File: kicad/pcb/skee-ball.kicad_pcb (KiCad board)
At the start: 2 copper layers, 106.8 x 104 mm, 61 parts, among them J13 HEADER, J18 DC_DRIVER, J19 JOYSTICK, J2 EXTERNAL_BUTTON, J20 SERVO, J21 US0, J22 US1, J26 US2, J27 US3, J3 Conn_02x06_Counter_Clockwise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

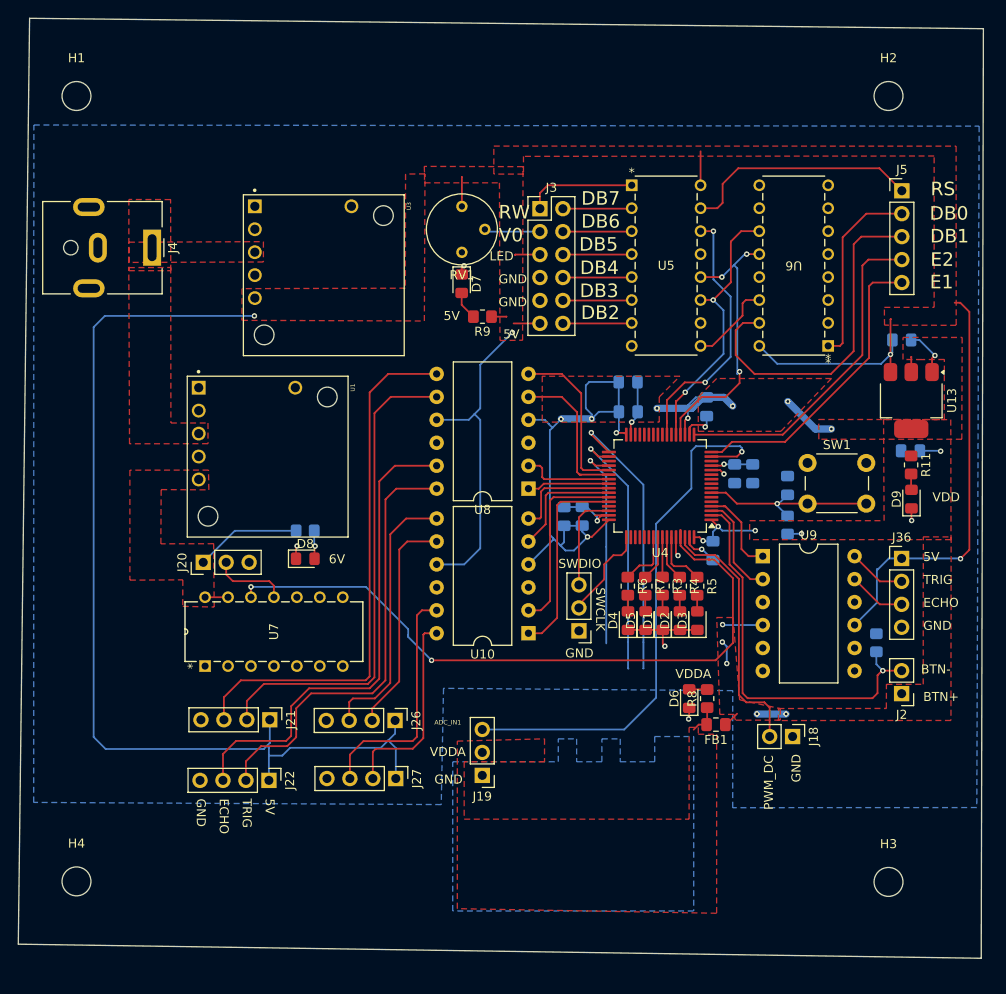
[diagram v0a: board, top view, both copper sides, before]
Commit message: only one drc error left
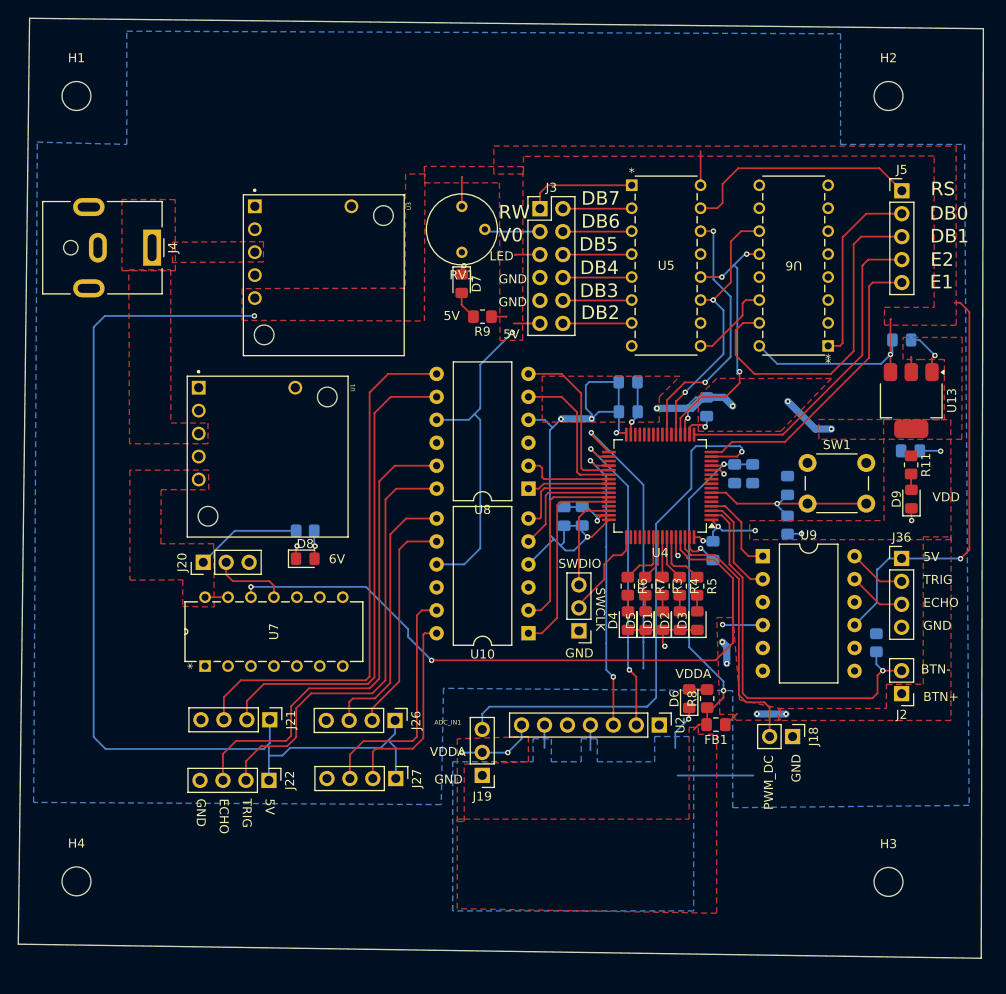
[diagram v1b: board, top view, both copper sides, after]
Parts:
- added U2: MAX98357A, Connector_PinHeader_2.54mm:PinHeader_1x07_P2.54mm_Vertical, F.Cu at (135.1, 99.1)
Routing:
- net VDDA: track 8.21 -> 48.2 mm, vias 1 -> 4
- net GND: track 44.2 -> 62.1 mm
- net SPI2-MOSI(I2S_SD): track 23.3 -> 32.7 mm, vias 1 -> 2
- net SPI2-SCK(I2S_CK): track 28.4 -> 34.8 mm, vias 1 -> 2
- net PWM_SERVO_3.3: track 76.4 -> 75.1 mm
- net ADC_IN1: track 59.5 -> 60.5 mm

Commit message: fix pcb dimensions
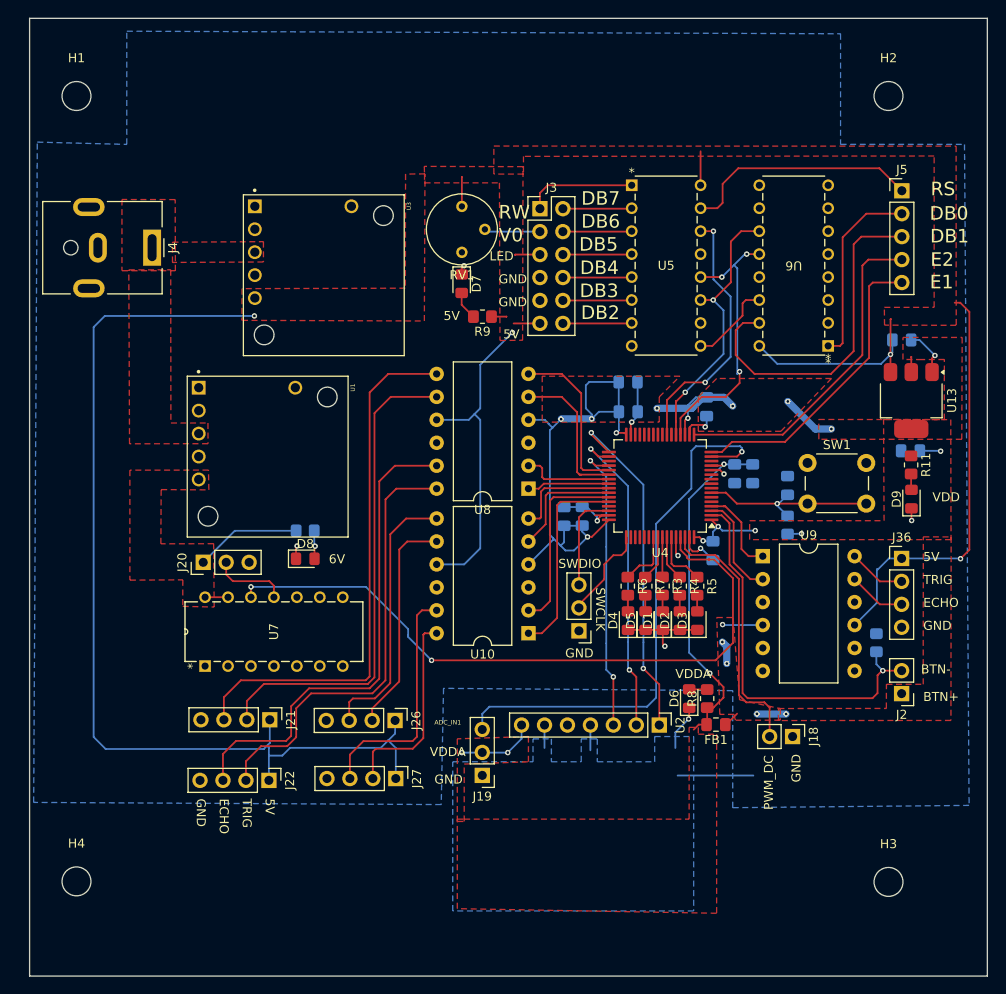
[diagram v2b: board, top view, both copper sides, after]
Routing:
- net SPI2-NSS(I2S_WS): track 31.4 -> 38.4 mm, vias 1 -> 2
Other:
- board size 106.8 x 104 mm -> 106 x 106 mm

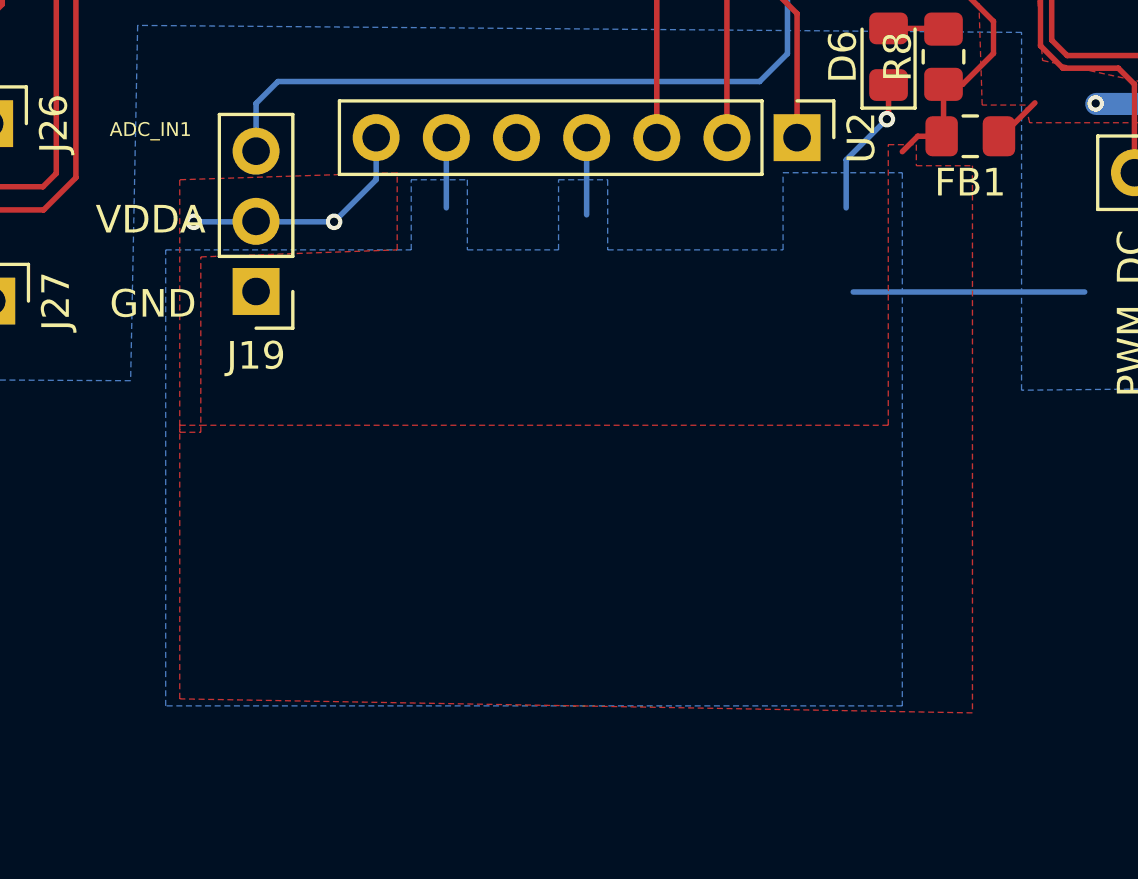
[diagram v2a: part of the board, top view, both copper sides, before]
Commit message: reorganize schematic and fix max98357a pins
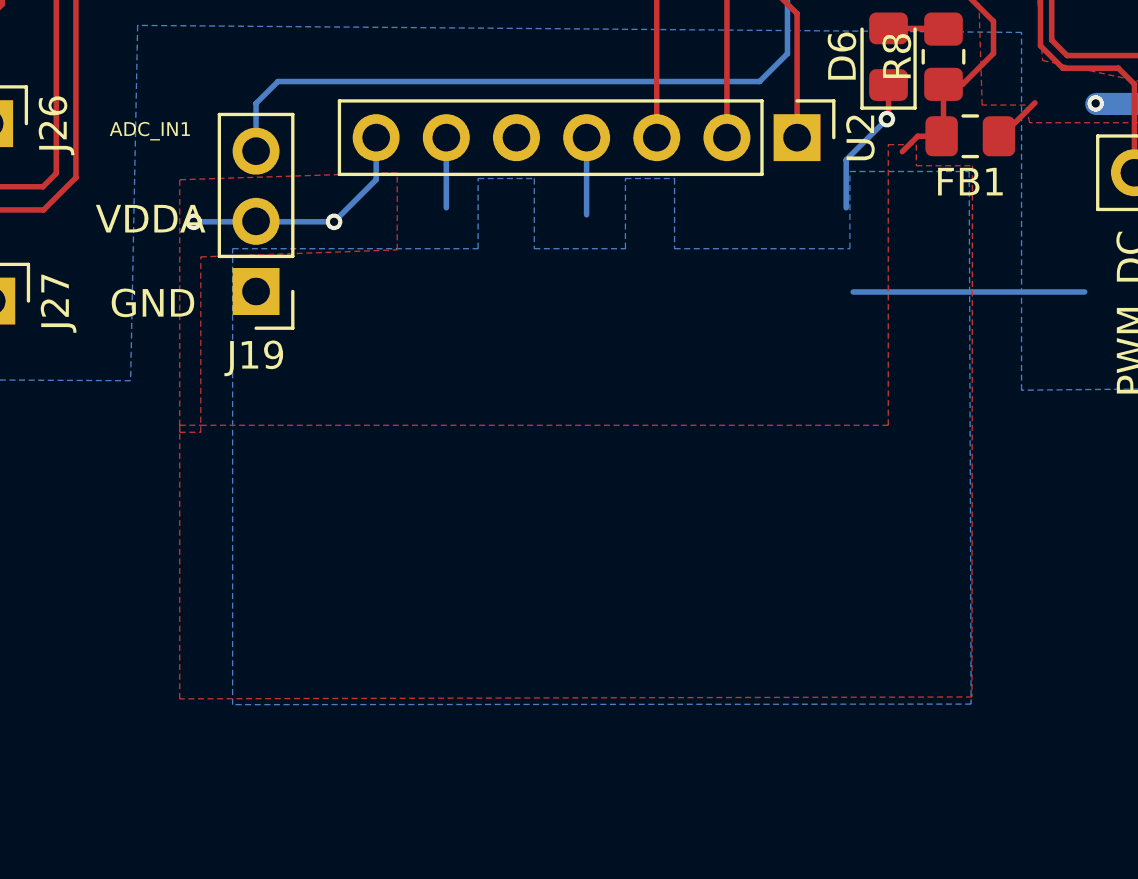
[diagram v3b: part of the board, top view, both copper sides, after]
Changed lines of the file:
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@@
 			(remove_unused_layers no)
 			(net 3 "GND")
-			(pinfunction "GAIN")
+			(pinfunction "GAIN_SLOT")
 			(pintype "passive")
 		)
@@
 		(min_thickness 0.25)
 		(filled_areas_thickness no)
-		(fill yes
+		(fill
 			(thermal_gap 0.5)
 			(thermal_bridge_width 0.5)
@@
 		(polygon
 			(pts
-				(xy 138.43 99.314) (xy 139.446 99.314) (xy 139.446 100.076) (xy 141.478 100.076) (xy 141.478 119.888)
+				(xy 138.43 99.314) (xy 139.446 99.314) (xy 139.446 100.076) (xy 141.478 100.076) (xy 141.46 119.31)
 				(xy 112.776 119.38) (xy 112.776 109.474) (xy 113.538 109.474) (xy 138.43 109.474)
 			)
@@
 		(min_thickness 0.25)
 		(filled_areas_thickness no)
-		(fill yes
+		(fill
 			(thermal_gap 0.5)
 			(thermal_bridge_width 0.5)
@@
 		(polygon
 			(pts
-				(xy 112.268 103.124) (xy 121.158 103.124) (xy 121.158 100.584) (xy 123.19 100.584) (xy 123.19 103.124)
-				(xy 126.492 103.124) (xy 126.492 100.584) (xy 128.27 100.584) (xy 128.27 103.124) (xy 134.62 103.124)
-				(xy 134.62 100.33) (xy 138.938 100.33) (xy 138.938 119.634) (xy 112.268 119.634)
+				(xy 114.69 103.08) (xy 123.58 103.08) (xy 123.58 100.54) (xy 125.612 100.54) (xy 125.612 103.08)
+				(xy 128.914 103.08) (xy 128.914 100.54) (xy 130.692 100.54) (xy 130.692 103.08) (xy 137.042 103.08)
+				(xy 137.042 100.286) (xy 141.36 100.286) (xy 141.43 119.57) (xy 114.69 119.59)
 			)
 		)

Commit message: update silk screen
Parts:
- moved H1 2.66 mm to (72.7, 27.7)
- moved H4 2.66 mm to (72.7, 114.7)
- moved H2 2.66 mm to (162.5, 27.7)
- moved H3 2.66 mm to (162.5, 114.7)
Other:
- board text added: "LED+"
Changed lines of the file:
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@@
 		(tags "LED handsolder")
 		(property "Reference" "D9"
-			(at 0 -1.65 90)
+			(at -1.05 2.71 0)
 			(layer "F.SilkS")
 			(effects
@@
 		(tags "LED handsolder")
 		(property "Reference" "D6"
-			(at 0 -1.65 90)
+			(at -0.07 -2.56 180)
 			(layer "F.SilkS")
 			(effects
@@
 	(footprint "MountingHole:MountingHole_3.2mm_M3"
 		(layer "F.Cu")
-		(at 70.63 29.44)
+		(at 72.67 27.74)
 		(descr "Mounting Hole 3.2mm, no annular, M3")
 		(tags "mounting hole 3.2mm no annular m3")
@@
 	(footprint "MountingHole:MountingHole_3.2mm_M3"
 		(layer "F.Cu")
-		(at 160.5 29.44)
+		(at 162.54 27.74)
 		(descr "Mounting Hole 3.2mm, no annular, M3")
 		(tags "mounting hole 3.2mm no annular m3")
@@
 			(at 0 -7.6 0)
 			(layer "F.SilkS")
+			(hide yes)
 			(effects
 				(font
@@
 	(footprint "MountingHole:MountingHole_3.2mm_M3"
 		(layer "F.Cu")
-		(at 160.5 116.42)
+		(at 162.54 114.72)
 		(descr "Mounting Hole 3.2mm, no annular, M3")
 		(tags "mounting hole 3.2mm no annular m3")
@@
 	(footprint "MountingHole:MountingHole_3.2mm_M3"
 		(layer "F.Cu")
-		(at 70.63 116.36)
+		(at 72.67 114.66)
 		(descr "Mounting Hole 3.2mm, no annular, M3")
 		(tags "mounting hole 3.2mm no annular m3")
@@
 		)
 	)
+	(gr_text "LED+"
+		(at 133.35 95.19 0)
+		(layer "F.SilkS")
+		(effects
+			(font
+				(size 1 1)
+				(thickness 0.1875)
+			)
+			(justify left bottom)
+		)
+	)
 	(gr_text "GND"
 		(at 117.348 52.832 0)
@@
 		)
 	)
+	(gr_text "LED+"
+		(at 108.12 49.81 0)
+		(layer "F.SilkS")
+		(effects
+			(font
+				(size 1 1)
+				(thickness 0.1875)
+			)
+			(justify left bottom)
+		)
+	)
 	(gr_text "RS"
 		(at 165.15 40.61 0)
@@
 	)
 	(gr_text "VDD"
-		(at 165.354 74.422 0)
+		(at 161.69 75.39 90)
 		(layer "F.SilkS")
 		(effects
@@
 		)
 	)
+	(gr_text "LED+"
+		(at 95.9 83.08 0)
+		(layer "F.SilkS")
+		(effects
+			(font
+				(size 1 1)
+				(thickness 0.1875)
+			)
+			(justify left bottom)
+		)
+	)
 	(gr_text "ADC_IN1"
 		(at 110.236 99.06 0)
@@
 		)
 	)
+	(gr_text "LED+"
+		(at 164.49 73.56 0)
+		(layer "F.SilkS")
+		(effects
+			(font
+				(size 1 1)
+				(thickness 0.1875)
+			)
+			(justify left bottom)
+		)
+	)
 	(gr_text "V0"
 		(at 117.348 45.72 0)
@@
 		(start 121.92 46.99)
 		(end 119.2 46.99)
-		(width 0.2)
+		(width 0.5)
 		(layer "F.Cu")
 		(net 39)
@@
 		(min_thickness 0.25)
 		(filled_areas_thickness no)
-		(fill
+		(fill yes
 			(thermal_gap 0.5)
 			(thermal_bridge_width 0.5)
@@
 		(min_thickness 0.25)
 		(filled_areas_thickness no)
-		(fill
+		(fill yes
 			(thermal_gap 0.5)
 			(thermal_bridge_width 0.5)
@@
 		(polygon
 			(pts
-				(xy 114.69 103.08) (xy 123.58 103.08) (xy 123.58 100.54) (xy 125.612 100.54) (xy 125.612 103.08)
-				(xy 128.914 103.08) (xy 128.914 100.54) (xy 130.692 100.54) (xy 130.692 103.08) (xy 137.042 103.08)
-				(xy 137.042 100.286) (xy 141.36 100.286) (xy 141.43 119.57) (xy 114.69 119.59)
+				(xy 112.49 103.23) (xy 121.38 103.23) (xy 121.38 100.69) (xy 123.412 100.69) (xy 123.412 103.23)
+				(xy 126.714 103.23) (xy 126.714 100.69) (xy 128.492 100.69) (xy 128.492 103.23) (xy 134.842 103.23)
+				(xy 134.842 100.436) (xy 139.16 100.436) (xy 139.23 119.72) (xy 112.49 119.74)
 			)
 		)
@@
 		(polygon
 			(pts
-				(xy 66.294 34.544) (xy 76.2 34.798) (xy 76.200289 22.270882) (xy 155.194191 22.552563) (xy 155.194 34.798)
+				(xy 66.294 34.544) (xy 78.8 34.72) (xy 78.820289 22.380882) (xy 155.194191 22.552563) (xy 155.194 34.798)
 				(xy 168.91 34.798) (xy 169.418 107.95) (xy 143.256 108.204) (xy 143.256 95.25) (xy 111.252 94.996)
 				(xy 110.998 107.860781) (xy 65.89 107.62)

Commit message: update revision number and sheet details
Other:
- board text added: "Revision #2"
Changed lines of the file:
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@@
 	)
 	(paper "A4")
+	(title_block
+		(title "Electronic Skee Ball")
+		(date "03/05/2025")
+		(rev "2")
+		(company "Purdue University")
+		(comment 1 "Created by Andrew Cali, David Fall, Jennifer Ferguson, and Madeline Flanagan for ECE 47700 Digital Systems Senior Design, Spring 2025.")
+	)
 	(layers
 		(0 "F.Cu" signal)
@@
 		(layer "Edge.Cuts")
 	)
+	(gr_text "Revision #2"
+		(at 108.43 115.56 0)
+		(layer "B.SilkS")
+		(effects
+			(font
+				(size 1.5 1.5)
+				(thickness 0.3)
+				(bold yes)
+			)
+			(justify left bottom mirror)
+		)
+	)
 	(gr_text "ECE 47700 Team #1\nElectronic Skee Ball\nSpring 2025"
